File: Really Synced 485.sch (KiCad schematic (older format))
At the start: 8 parts

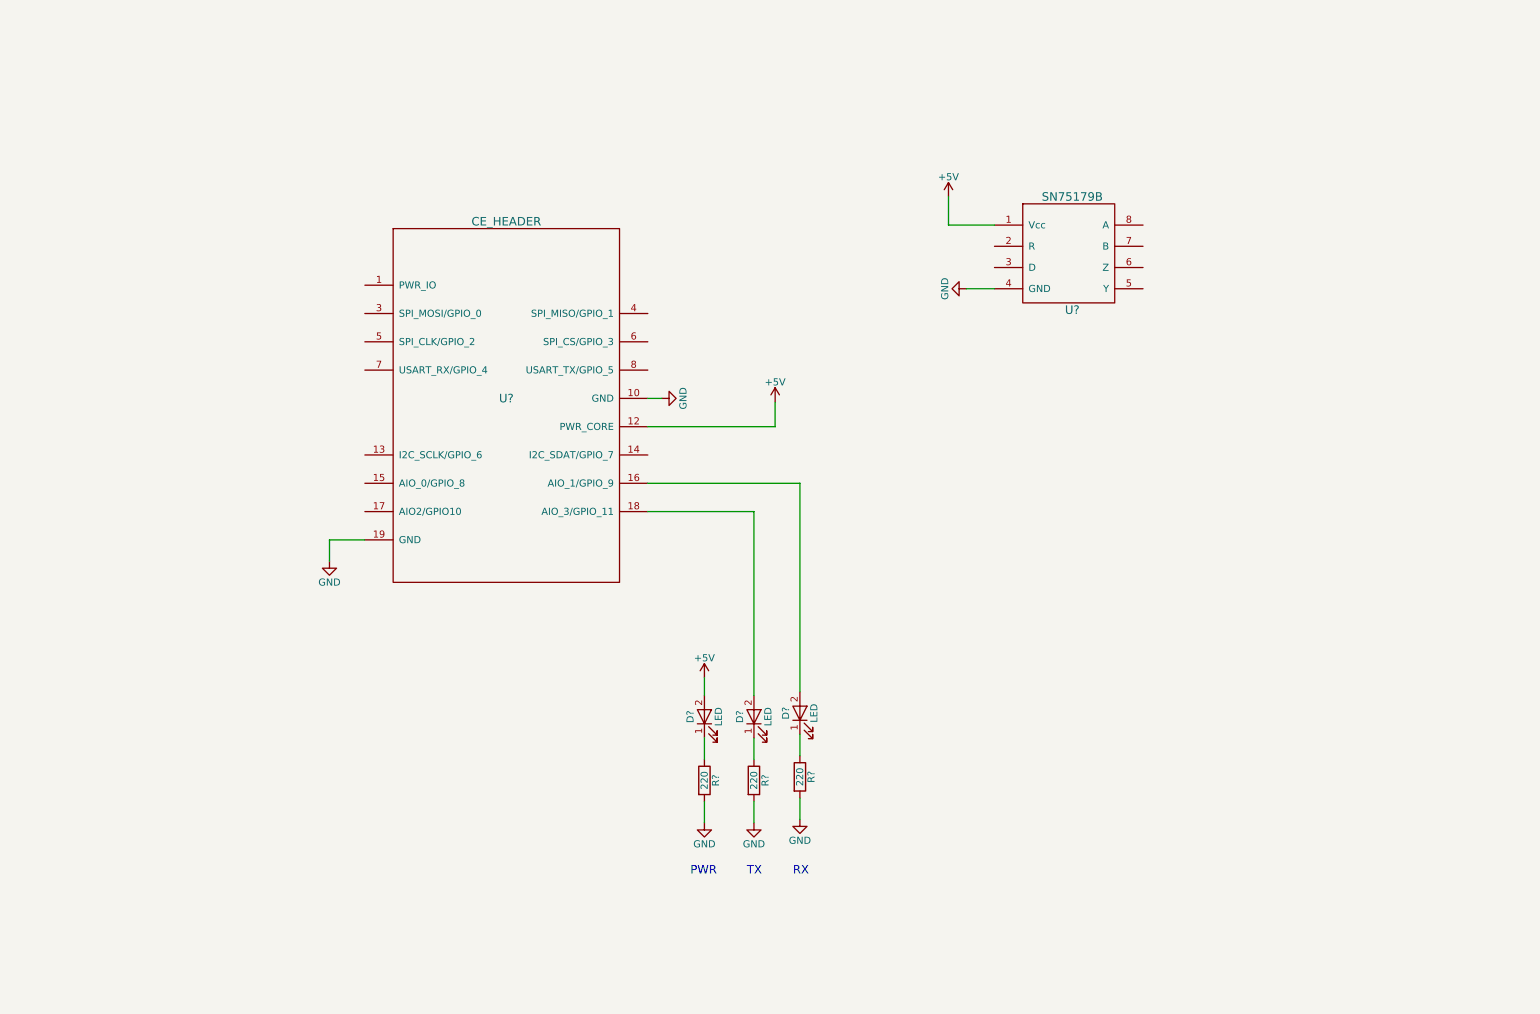
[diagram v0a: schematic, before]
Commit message: Finished schematic with piano switch and ethernet jack
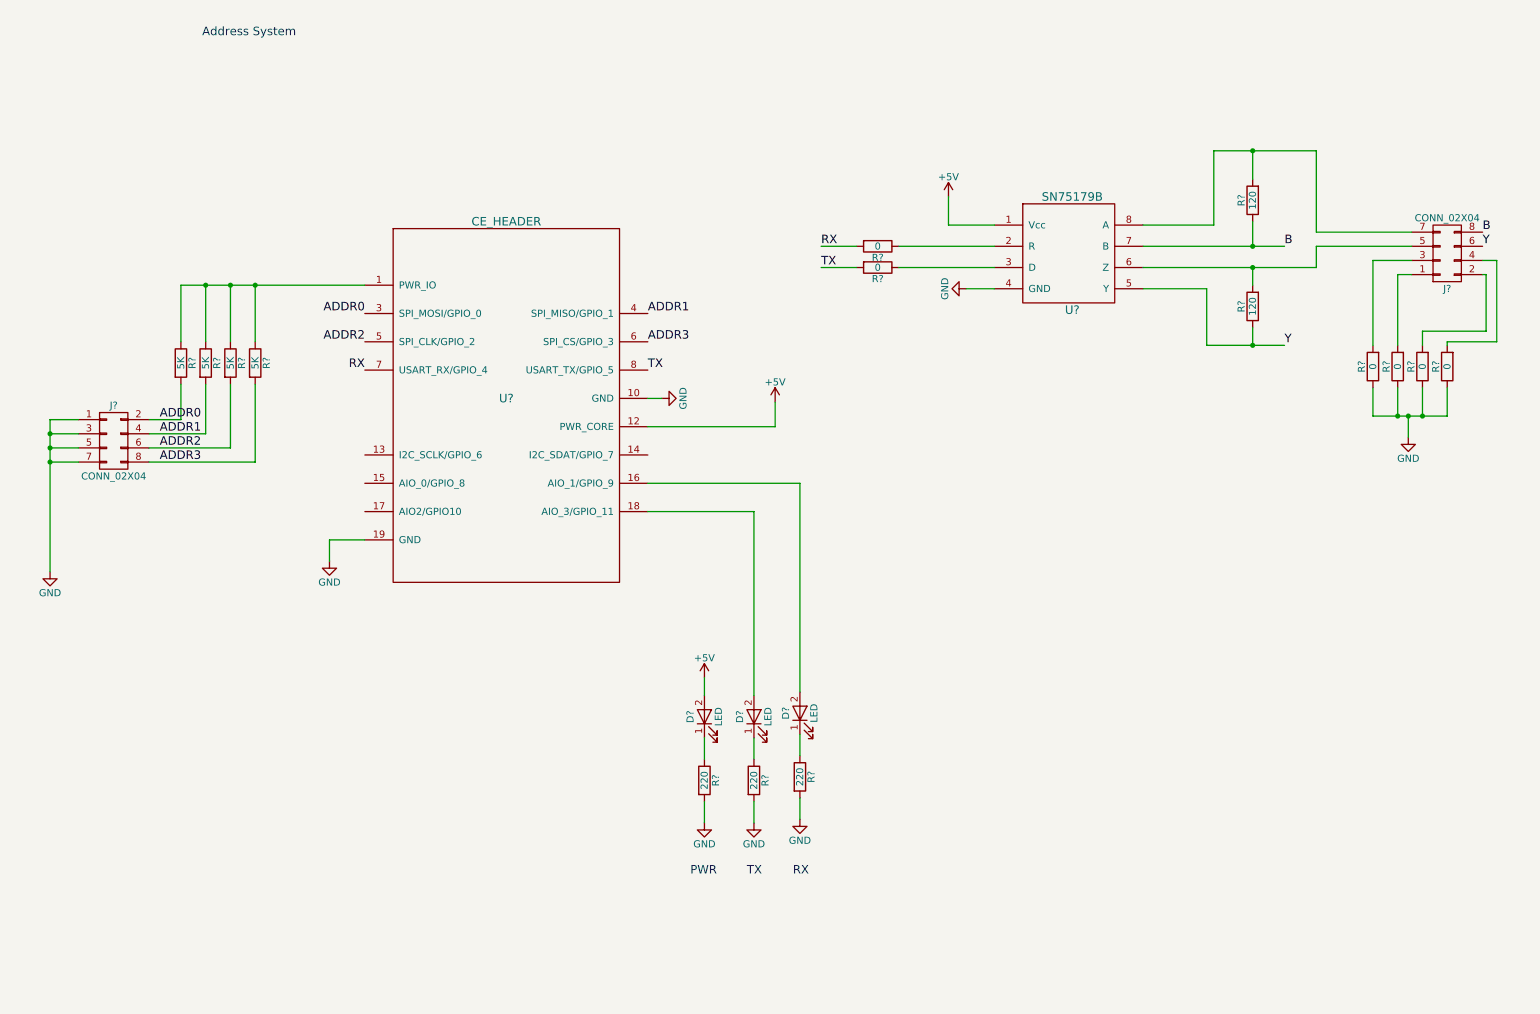
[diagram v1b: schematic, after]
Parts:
- added J? (x2): CONN_02X04, symbol CONN_02X04
- added R? (x6): 0, symbol R
- added R? (x2): 120, symbol R
- added R? (x4): 5K, symbol R
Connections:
- net GND: now also J?.1 (P1), J?.3 (P3), J?.5 (P5), J?.7 (P7), R?.1, R?.1, R?.1, R?.1
- net at U?.1 (PWR_IO): now also R?.1, R?.1, R?.1, R?.1
- net ADDR0: now reaches U?.3 (SPI_MOSI/GPIO_0)
- net ADDR0: now also J?.2 (P2), R?.2
- net ADDR1: now reaches U?.4 (SPI_MISO/GPIO_1)
- net ADDR1: now also J?.4 (P4), R?.2
- net ADDR2: now reaches U?.5 (SPI_CLK/GPIO_2)
- net ADDR2: now also J?.6 (P6), R?.2
- net ADDR3: now reaches U?.6 (SPI_CS/GPIO_3)
- net ADDR3: now also J?.8 (P8), R?.2
- net RX: now reaches U?.7 (USART_RX/GPIO_4)
- net RX: now also R?.2
- net TX: now reaches U?.8 (USART_TX/GPIO_5)
- net TX: now also R?.2
- net at U?.2 (R): now also R?.1
- net at U?.3 (D): now also R?.1
- net Y: now reaches U?.5 (Y)
- net Y: now also J?.6 (P6), R?.1
- net at U?.6 (Z): now also J?.5 (P5), R?.2
- net B: now reaches U?.7 (B)
- net B: now also J?.8 (P8), R?.1
- net at U?.8 (A): now also J?.7 (P7), R?.2
- new net: J?.1 (P1), R?.2
- new net: J?.2 (P2), R?.2
- new net: J?.3 (P3), R?.2
- new net: J?.4 (P4), R?.2
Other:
- note added: "Address System"

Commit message: Added half duplex circuit and jumpers for switching between them
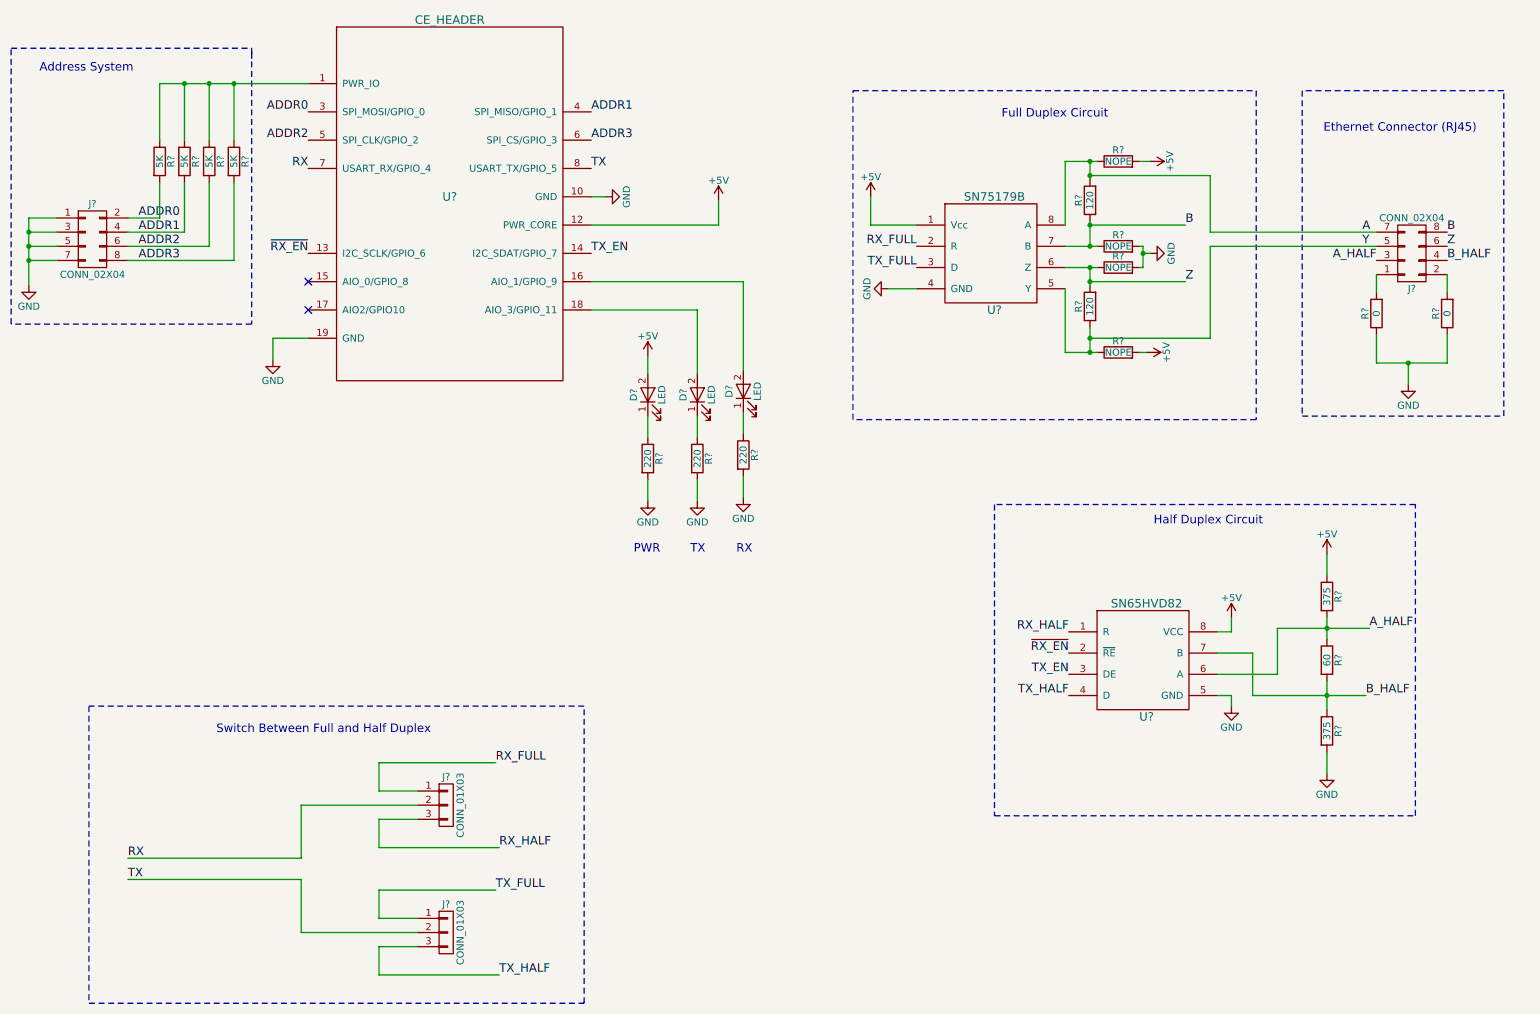
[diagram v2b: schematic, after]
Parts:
- removed R? (x4): 0, symbol R
- removed R?: 120, symbol R
- added J? (x2): CONN_01X03, symbol CONN_01X03
- added R?: 60, symbol R
- added R? (x2): 375, symbol R
- added R? (x4): NOPE, symbol R
- added R?: 120, symbol R
- added U?: SN65HVD82, symbol SN65HVD82
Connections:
- net +5V: now also R?.1, R?.2, R?.2, U?.8 (VCC)
- net B: now also R?.1, R?.1
- net GND: now also R?.2, R?.2, R?.2, U?.5 (GND)
- net RX: now also J?.2 (P2)
- net TX: now also J?.2 (P2)
- net Y: now also J?.5 (P5), R?.1; no longer J?.6 (P6)
- net ~RX_EN: now reaches U?.13 (I2C_SCLK/GPIO_6)
- net ~RX_EN: now also U?.2 (~RE)
- net TX_EN: now reaches U?.14 (I2C_SDAT/GPIO_7)
- net TX_EN: now also U?.3 (DE)
- net RX_FULL: now reaches U?.2 (R)
- net RX_FULL: now also J?.1 (P1)
- net TX_FULL: now reaches U?.3 (D)
- net TX_FULL: now also J?.1 (P1)
- net Z: now reaches R?.2, U?.6 (Z)
- net Z: now also J?.6 (P6), R?.1; no longer J?.5 (P5)
- net A: now reaches J?.7 (P7), U?.8 (A)
- net A: now also R?.1, R?.2
- net at J?.1 (P1): now also R?.2
- net at J?.2 (P2): now also R?.2
- net A_HALF: now reaches J?.3 (P3)
- net A_HALF: now also R?.1, R?.2, U?.6 (A); no longer R?.2
- net B_HALF: now reaches J?.4 (P4)
- net B_HALF: now also R?.1, R?.2, U?.7 (B); no longer R?.2
- new net RX_HALF: J?.3 (P3), U?.1 (R)
- new net TX_HALF: J?.3 (P3), U?.4 (D)
- no-connect marks 0 -> 2
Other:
- note added: "Ethernet Connector (RJ45)"
- note added: "Full Duplex Circuit"
- note added: "Half Duplex Circuit"
- note added: "Switch Between Full and Half Duplex"
- moved on the sheet: D?, J?, R?, U?

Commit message: Finished schematic
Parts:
- added D? (x2): LED, symbol LED
- added R? (x2): 220, symbol R
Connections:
- net GND: now also R?.2, R?.2
- net RX: now also D?.2 (A)
- net TX: now also D?.2 (A)
- net at U?.16 (AIO_1/GPIO_9): now also D?.2 (A); no longer D?.2 (A)
- net at U?.18 (AIO_3/GPIO_11): now also D?.2 (A); no longer D?.2 (A)
- new net: D?.1 (K), R?.1 (x2)
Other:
- note added: "STATUS1"
- note added: "STATUS2"
- note removed: "RX"
- note removed: "TX"
- moved on the sheet: D?, J?, R?

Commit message: Annotated schematic
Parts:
- added C? (x2): .1U, symbol C
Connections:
- net +5V: now also C?.1, C?.2
- net GND: now also C?.1, C?.2
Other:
- note added: "Piano Switch"
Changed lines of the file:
@@
-$Comp
-L GND #PWR?
-U 1 1 592B9AE4
-P 6775 2450
-F 0 "#PWR?" H 6775 2200 50  0001 C CNN
-F 1 "GND" H 6775 2300 50  0000 C CNN
-F 2 "" H 6775 2450 50  0001 C CNN
-F 3 "" H 6775 2450 50  0001 C CNN
-	1    6775 2450
-	0    1    1    0
-$EndComp
 $Comp
 L GND #PWR?
@@
 L +5V #PWR?
 U 1 1 592CCFBB
-P 9200 4775
-F 0 "#PWR?" H 9200 4625 50  0001 C CNN
-F 1 "+5V" H 9200 4915 50  0000 C CNN
-F 2 "" H 9200 4775 50  0001 C CNN
-F 3 "" H 9200 4775 50  0001 C CNN
-	1    9200 4775
+P 9200 4375
+F 0 "#PWR?" H 9200 4225 50  0001 C CNN
+F 1 "+5V" H 9200 4515 50  0000 C CNN
+F 2 "" H 9200 4375 50  0001 C CNN
+F 3 "" H 9200 4375 50  0001 C CNN
+	1    9200 4375
 	1    0    0    -1
 $EndComp
@@
 Text Notes 9850 1350 0    60   ~ 0
 Ethernet Connector (RJ45)
-Text Notes 7575 1250 0    60   ~ 0
+Text Notes 7050 1125 0    60   ~ 0
 Full Duplex Circuit
 $Comp
@@
 	4775 1800 4675 1800
 Wire Wire Line
-	6975 2450 6775 2450
+	6400 2450 6975 2450
 Wire Wire Line
 	2425 2950 2425 2800
@@
 	2275 750  2275 825
 Wire Wire Line
-	9200 4775 9200 4875
+	9200 4375 9200 4875
 Wire Wire Line
 	9200 4875 9100 4875
@@
 Wire Notes Line
 	9700 1050 9700 3350
-Wire Notes Line
-	9375 1050 9375 3375
-Wire Notes Line
-	9375 3375 6525 3375
-Wire Notes Line
-	6525 3375 6525 1050
-Wire Notes Line
-	6525 1050 9375 1050
 Text Notes 8650 4125 0    60   ~ 0
 Half Duplex Circuit
@@
 Text Notes 5700 4325 0    60   ~ 0
 STATUS2
+Wire Notes Line
+	4350 4100 4350 6900
+Wire Notes Line
+	4350 6900 850  6900
+Wire Notes Line
+	850  4100 4350 4100
+Wire Notes Line
+	850  6900 850  4100
+$Comp
+L C C?
+U 1 1 592EAC9B
+P 6425 2175
+F 0 "C?" H 6450 2275 50  0000 L CNN
+F 1 ".1U" H 6450 2075 50  0000 L CNN
+F 2 "" H 6463 2025 50  0001 C CNN
+F 3 "" H 6425 2175 50  0001 C CNN
+	1    6425 2175
+	1    0    0    -1
+$EndComp
+Wire Wire Line
+	6425 2025 6425 1900
+Wire Wire Line
+	6425 1900 6650 1900
+Connection ~ 6650 1900
+Wire Wire Line
+	6425 2325 6425 2450
+Connection ~ 6425 2450
+$Comp
+L GND #PWR?
+U 1 1 592EB45E
+P 6400 2450
+F 0 "#PWR?" H 6400 2200 50  0001 C CNN
+F 1 "GND" H 6400 2300 50  0000 C CNN
+F 2 "" H 6400 2450 50  0001 C CNN
+F 3 "" H 6400 2450 50  0001 C CNN
+	1    6400 2450
+	0    1    1    0
+$EndComp
+$Comp
+L C C?
+U 1 1 592EBB05
+P 9375 4600
+F 0 "C?" H 9400 4700 50  0000 L CNN
+F 1 ".1U" H 9400 4500 50  0000 L CNN
+F 2 "" H 9413 4450 50  0001 C CNN
+F 3 "" H 9375 4600 50  0001 C CNN
+	1    9375 4600
+	-1   0    0    1
+$EndComp
+$Comp
+L GND #PWR?
+U 1 1 592EC2B7
+P 9375 4800
+F 0 "#PWR?" H 9375 4550 50  0001 C CNN
+F 1 "GND" H 9375 4650 50  0000 C CNN
+F 2 "" H 9375 4800 50  0001 C CNN
+F 3 "" H 9375 4800 50  0001 C CNN
+	1    9375 4800
+	1    0    0    -1
+$EndComp
+Wire Wire Line
+	9375 4800 9375 4750
+Wire Wire Line
+	9375 4450 9375 4400
+Wire Wire Line
+	9375 4400 9200 4400
+Connection ~ 9200 4400
+Text Notes 1025 2525 0    60   ~ 0
+Piano Switch
+Wire Notes Line
+	9150 750  9150 3375
+Wire Notes Line
+	9150 3375 6150 3375
+Wire Notes Line
+	6150 3375 6150 750
+Wire Notes Line
+	6150 750  9150 750
 $EndSCHEMATC

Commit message: Mostly associated, need to make some footprints
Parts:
- gave numbers to parts that had none: 34

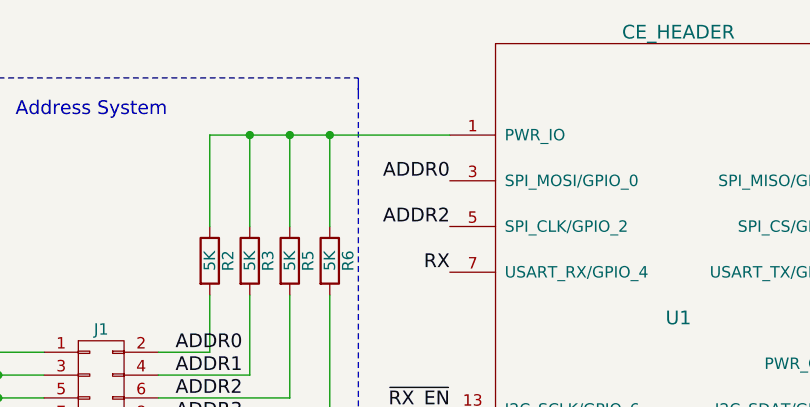
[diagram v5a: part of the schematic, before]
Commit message: Finished piano switch layout
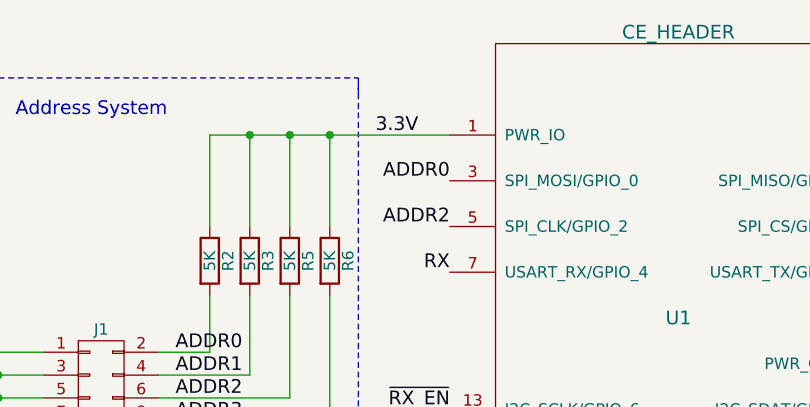
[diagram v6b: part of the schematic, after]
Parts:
- C1, C2: footprint (none) -> Capacitors_SMD:C_0805
- D1, D2, D3, D4, D5: footprint (none) -> LEDs:LED_0805
- J1: footprint (none) -> ReallySynced:195-4MST
- J2, J3: footprint (none) -> Pin_Headers:Pin_Header_Straight_1x03_Pitch2.54mm
- J4: footprint (none) -> ReallySynced:54602-908LF
- R1, R10, R11, R12, R13, R14, R15, R16, R17, R18, R19, R2, R20, R3, R4, R5, R6, R7, R8, R9: footprint (none) -> Resistors_SMD:R_0805_HandSoldering
- U1: footprint (none) -> ReallySynced:CE_Header
- U2, U3: footprint (none) -> Housings_SOIC:SOIC-8_3.9x4.9mm_Pitch1.27mm
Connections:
- net 3.3V: now reaches R2.1, R3.1, R5.1, R6.1, U1.1 (PWR_IO)

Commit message: Updated MPN/link for half duplex driver
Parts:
- U3: Link (none) -> http://www.digikey.com/scripts/DkSearch/dksus.dll?Detail&it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; MPN (none) -> SN65HVD82DR
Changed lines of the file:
@@
 F 2 "Housings_SOIC:SOIC-8_3.9x4.9mm_Pitch1.27mm" H 8550 4975 60  0001 C CNN
 F 3 "" H 8550 4975 60  0001 C CNN
+F 4 "SN65HVD82DR" H 8600 5075 60  0001 C CNN "MPN"
+F 5 "http://www.digikey.com/scripts/DkSearch/dksus.dll?Detail&itemSeq=229385765&uq=636318288619921391" H 8600 5075 60  0001 C CNN "Link"
 	1    8600 5075
 	1    0    0    -1
